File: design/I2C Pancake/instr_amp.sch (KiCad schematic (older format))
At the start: 5 parts, among them J4 Conn_01x04, U3 INA826

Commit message: Create initial 4-layer routing for I2C Pancake Board.
This is my first attempt at doing 4-layer routing. There are
some outstanding issues with the routing here. Namely, the
coupling/decoupling capacitors have rather long traces
connecting them to their respective devices. These issues
will be fixed in future commits.
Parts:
- C5: symbol i2c_pancake-rescue:C-device -> i2c_pancake-rescue:C-device-i2c_pancake-rescue
- J4: symbol i2c_pancake-rescue:Conn_01x04-strain_gauges_rtr-rescue -> i2c_pancake-rescue:Conn_01x04-strain_gauges_rtr-rescue-i2c_pancake-rescue
- R6, R7: symbol i2c_pancake-rescue:R-device -> i2c_pancake-rescue:R-device-i2c_pancake-rescue
- U3: symbol i2c_pancake-rescue:INA826-daq_components -> i2c_pancake-rescue:INA826-daq_components-i2c_pancake-rescue
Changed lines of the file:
@@
 $EndDescr
 $Comp
-L i2c_pancake-rescue:INA826-daq_components U3
+L i2c_pancake-rescue:INA826-daq_components-i2c_pancake-rescue U3
 U 1 1 5ACAFA52
 P 5900 4100
@@
 $EndComp
 $Comp
-L i2c_pancake-rescue:Conn_01x04-strain_gauges_rtr-rescue J4
+L i2c_pancake-rescue:Conn_01x04-strain_gauges_rtr-rescue-i2c_pancake-rescue J4
 U 1 1 5ACAFAD2
 P 4750 3150
@@
 	5100 3350 4950 3350
 $Comp
-L i2c_pancake-rescue:R-device R6
+L i2c_pancake-rescue:R-device-i2c_pancake-rescue R6
 U 1 1 5ACAFBC2
 P 5000 4100
@@
 	6450 3950 6350 3950
 $Comp
-L i2c_pancake-rescue:C-device C5
+L i2c_pancake-rescue:C-device-i2c_pancake-rescue C5
 U 1 1 5ACAFF7B
 P 6600 3700
@@
 AR Path="/5ACB084A/5ACAFF7B" Ref="C8"  Part="1"
 AR Path="/5E82A218/5ACAFF7B" Ref="C2"  Part="1"
+AR Path="/5ACAFF7B" Ref="C2"  Part="1"
 F 0 "C2" V 6650 3750 50  0000 L CNN
 F 1 "0.1uF" V 6550 3750 50  0000 L CNN
@@
 G = 1 + 49.4K/RG
 $Comp
-L i2c_pancake-rescue:R-device R7
+L i2c_pancake-rescue:R-device-i2c_pancake-rescue R7
 U 1 1 5ACB2059
 P 6500 4150

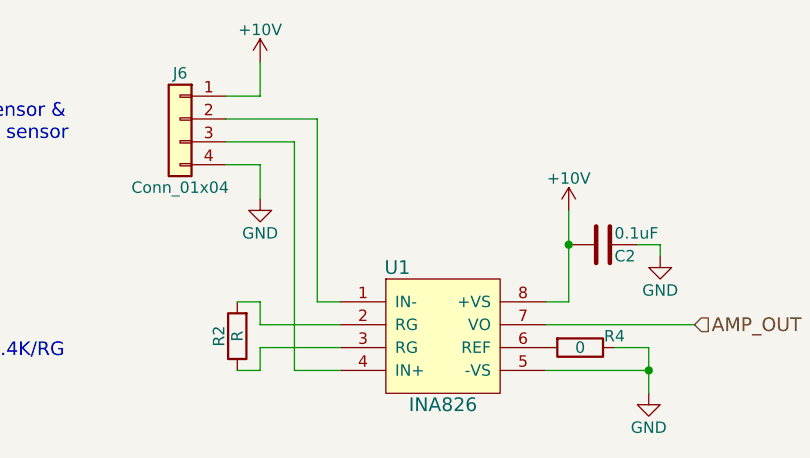
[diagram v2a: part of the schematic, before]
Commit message: Replace fuse footprint with standard 0805 SMD footprint.
A note has been added to the schematic regarding expected current
and trip current through the fuse.
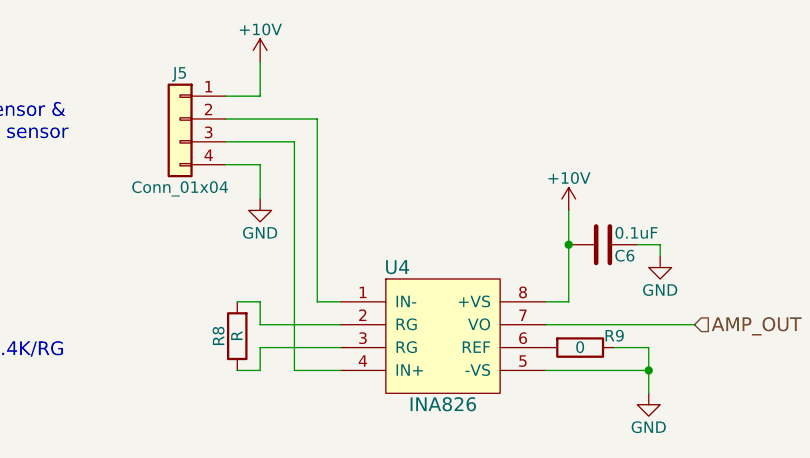
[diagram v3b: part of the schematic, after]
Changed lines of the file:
@@
 $Descr A4 11693 8268
 encoding utf-8
-Sheet 4 4
+Sheet 3 4
 Title ""
 Date ""
@@
 AR Path="/5ACB084A/5ACAFA52" Ref="U6"  Part="1"
 AR Path="/5E82A218/5ACAFA52" Ref="U1"  Part="1"
-F 0 "U1" H 5700 4400 60  0000 C CNN
+F 0 "U4" H 5700 4400 60  0000 C CNN
 F 1 "INA826" H 5900 3800 60  0000 C CNN
 F 2 "footprints:SOIC-8_3.9x4.9mm_Pitch1.27mm_HandSoldering" H 6050 3800 60  0001 C CNN
@@
 AR Path="/5ACB084A/5ACAFAD2" Ref="J7"  Part="1"
 AR Path="/5E82A218/5ACAFAD2" Ref="J6"  Part="1"
-F 0 "J6" H 4750 3350 50  0000 C CNN
+F 0 "J5" H 4750 3350 50  0000 C CNN
 F 1 "Conn_01x04" H 4750 2850 50  0000 C CNN
 F 2 "TerminalBlock_Phoenix:TerminalBlock_Phoenix_MKDS-1,5-4_1x04_P5.00mm_Horizontal" H 4750 3150 50  0001 C CNN
@@
 AR Path="/5ACB084A/5ACAFBC2" Ref="R12"  Part="1"
 AR Path="/5E82A218/5ACAFBC2" Ref="R2"  Part="1"
-F 0 "R2" V 5080 4100 50  0000 C CNN
+F 0 "R8" V 5080 4100 50  0000 C CNN
 F 1 "R" V 5000 4100 50  0000 C CNN
 F 2 "footprints:R_0805_HandSoldering" V 4930 4100 50  0001 C CNN
@@
 AR Path="/5E82A218/5ACAFF7B" Ref="C2"  Part="1"
 AR Path="/5ACAFF7B" Ref="C2"  Part="1"
-F 0 "C2" V 6650 3750 50  0000 L CNN
+F 0 "C6" V 6650 3750 50  0000 L CNN
 F 1 "0.1uF" V 6550 3750 50  0000 L CNN
 F 2 "footprints:C_0805_HandSoldering" H 6638 3550 50  0001 C CNN
@@
 AR Path="/5ACB084A/5ACB2059" Ref="R13"  Part="1"
 AR Path="/5E82A218/5ACB2059" Ref="R4"  Part="1"
-F 0 "R4" V 6450 4300 50  0000 C CNN
+F 0 "R9" V 6450 4300 50  0000 C CNN
 F 1 "0" V 6500 4150 50  0000 C CNN
 F 2 "footprints:R_0805_HandSoldering" V 6430 4150 50  0001 C CNN

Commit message: Add test points to the Pancake board.
Test points were added to the outputs of each strain guage amp.
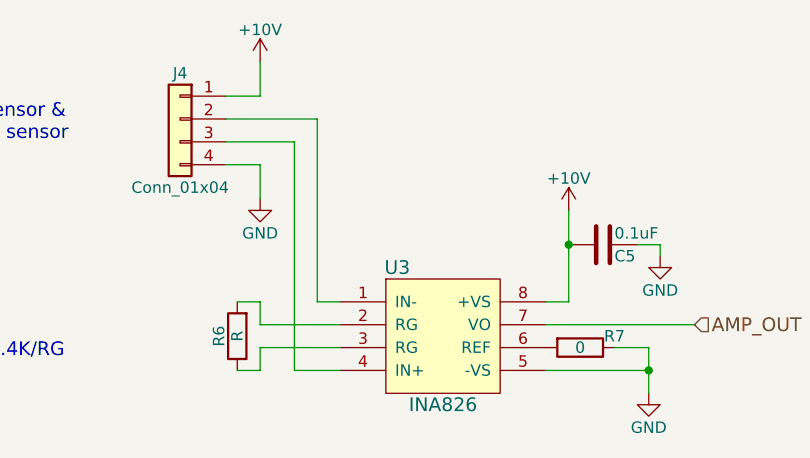
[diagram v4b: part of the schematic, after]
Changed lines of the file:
@@
 $Descr A4 11693 8268
 encoding utf-8
-Sheet 3 4
+Sheet 2 4
 Title ""
 Date ""
@@
 AR Path="/5ACB084A/5ACAFA52" Ref="U6"  Part="1"
 AR Path="/5E82A218/5ACAFA52" Ref="U1"  Part="1"
-F 0 "U4" H 5700 4400 60  0000 C CNN
+F 0 "U3" H 5700 4400 60  0000 C CNN
 F 1 "INA826" H 5900 3800 60  0000 C CNN
 F 2 "footprints:SOIC-8_3.9x4.9mm_Pitch1.27mm_HandSoldering" H 6050 3800 60  0001 C CNN
@@
 AR Path="/5ACB084A/5ACAFAD2" Ref="J7"  Part="1"
 AR Path="/5E82A218/5ACAFAD2" Ref="J6"  Part="1"
-F 0 "J5" H 4750 3350 50  0000 C CNN
+F 0 "J4" H 4750 3350 50  0000 C CNN
 F 1 "Conn_01x04" H 4750 2850 50  0000 C CNN
 F 2 "TerminalBlock_Phoenix:TerminalBlock_Phoenix_MKDS-1,5-4_1x04_P5.00mm_Horizontal" H 4750 3150 50  0001 C CNN
@@
 AR Path="/5ACB084A/5ACAFBC2" Ref="R12"  Part="1"
 AR Path="/5E82A218/5ACAFBC2" Ref="R2"  Part="1"
-F 0 "R8" V 5080 4100 50  0000 C CNN
+F 0 "R6" V 5080 4100 50  0000 C CNN
 F 1 "R" V 5000 4100 50  0000 C CNN
 F 2 "footprints:R_0805_HandSoldering" V 4930 4100 50  0001 C CNN
@@
 AR Path="/5E82A218/5ACAFF7B" Ref="C2"  Part="1"
 AR Path="/5ACAFF7B" Ref="C2"  Part="1"
-F 0 "C6" V 6650 3750 50  0000 L CNN
+F 0 "C5" V 6650 3750 50  0000 L CNN
 F 1 "0.1uF" V 6550 3750 50  0000 L CNN
 F 2 "footprints:C_0805_HandSoldering" H 6638 3550 50  0001 C CNN
@@
 AR Path="/5ACB084A/5ACB2059" Ref="R13"  Part="1"
 AR Path="/5E82A218/5ACB2059" Ref="R4"  Part="1"
-F 0 "R9" V 6450 4300 50  0000 C CNN
+F 0 "R7" V 6450 4300 50  0000 C CNN
 F 1 "0" V 6500 4150 50  0000 C CNN
 F 2 "footprints:R_0805_HandSoldering" V 6430 4150 50  0001 C CNN

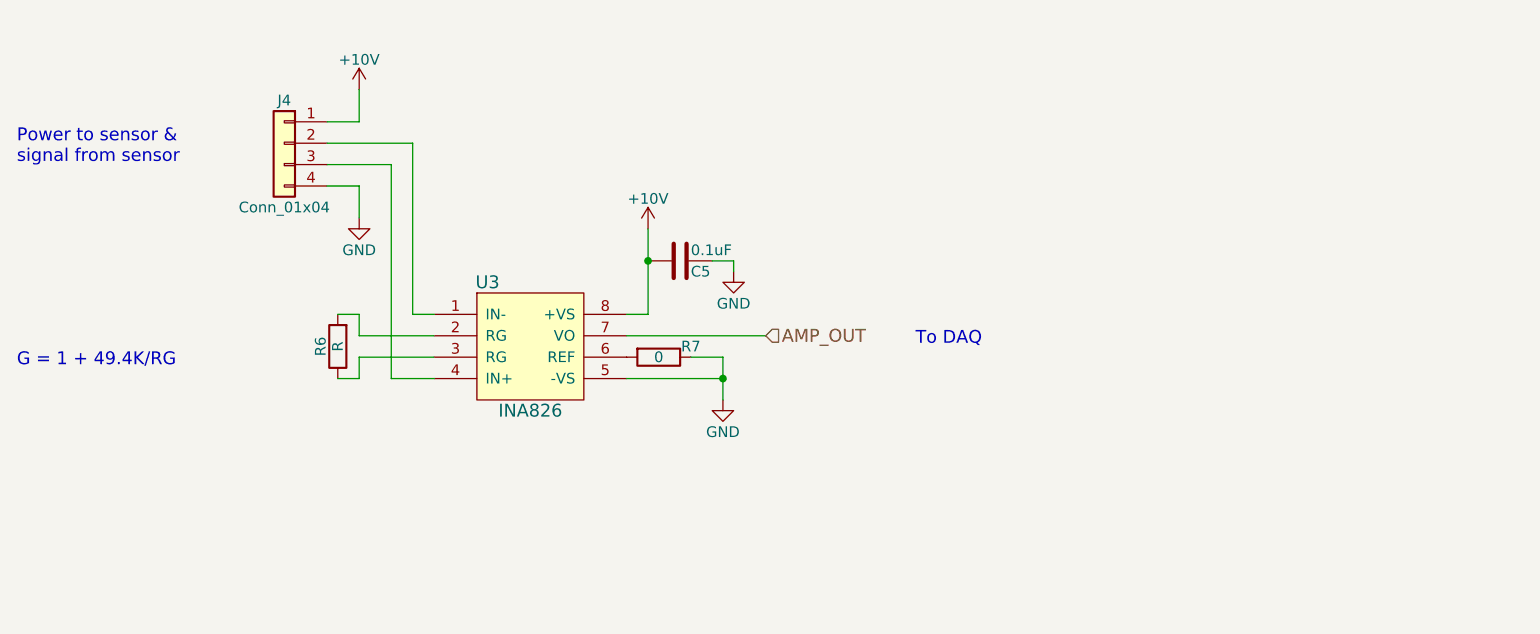
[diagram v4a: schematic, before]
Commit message: Implement improvements suggested by Zachariah Mears and update Gerbers
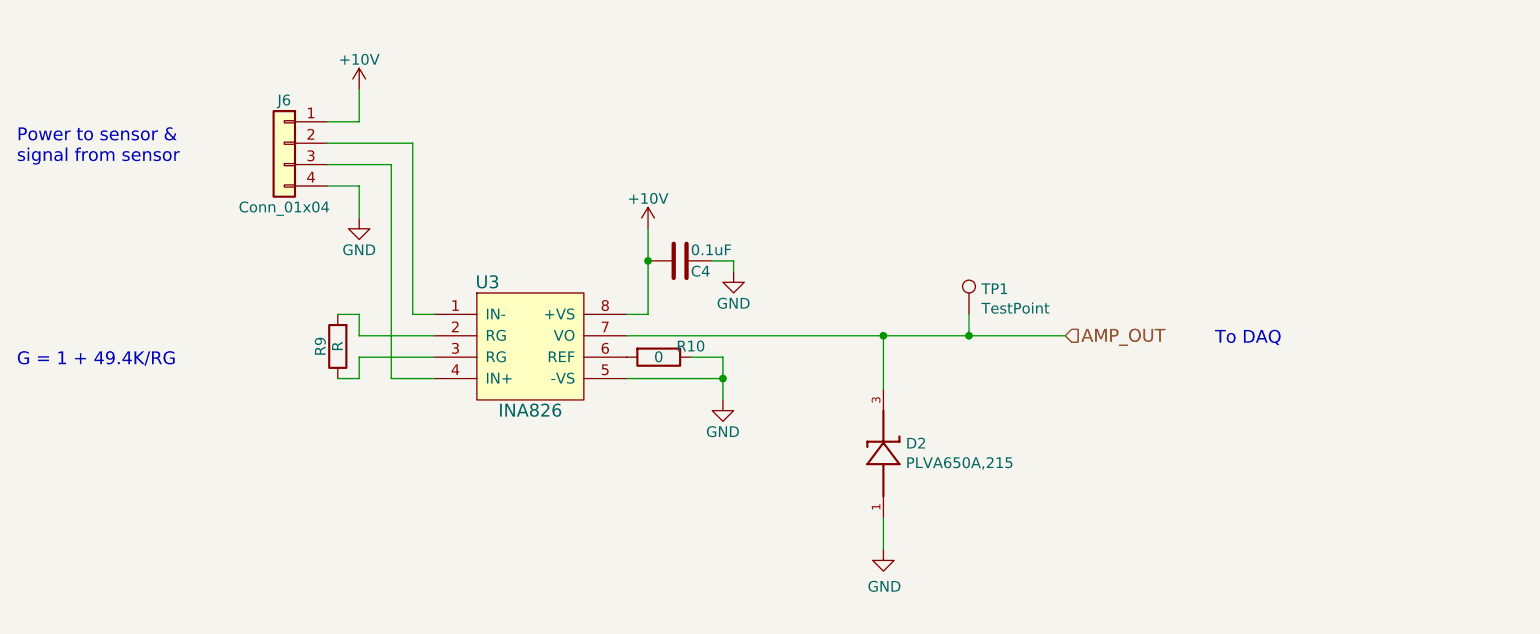
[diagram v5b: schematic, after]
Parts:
- added D2: PLVA650A,215, footprints:SOT95P230X110-3N, symbol PLVA650A_215:PLVA650A,215
- added TP1: TestPoint, custom:TestPoint, symbol Connector:TestPoint
- renumbered C5 to C4, J4 to J6, R7 to R10, R6 to R9
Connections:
- net AMP_OUT: now also D2.3, TP1.1
- net GND: now also D2.1

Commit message: Replace linear regulator to match the recent Digikey order
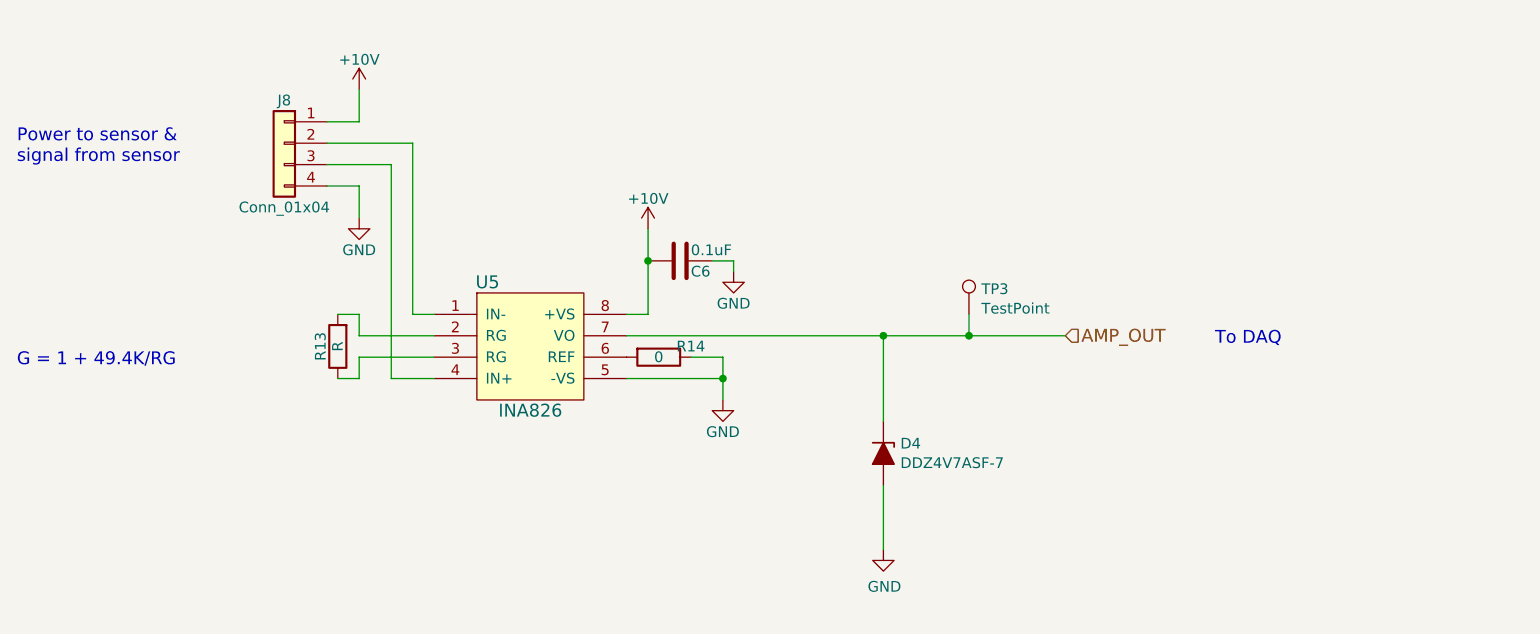
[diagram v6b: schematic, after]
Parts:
- removed D2: PLVA650A,215, footprints:SOT95P230X110-3N, symbol PLVA650A_215:PLVA650A,215
- added D2: DDZ4V7ASF-7, Diode_SMD:D_SOD-323F, symbol Device:D_Zener_ALT
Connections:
- net AMP_OUT: now also D2.1 (K)
- net GND: now also D2.2 (A)
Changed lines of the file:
@@
 $Descr A4 11693 8268
 encoding utf-8
-Sheet 2 4
+Sheet 4 4
 Title ""
 Date ""
@@
 AR Path="/5ACB084A/5ACAFA52" Ref="U?"  Part="1"
 AR Path="/5E82A218/5ACAFA52" Ref="U5"  Part="1"
-F 0 "U3" H 5700 4400 60  0000 C CNN
+F 0 "U5" H 5700 4400 60  0000 C CNN
 F 1 "INA826" H 5900 3800 60  0000 C CNN
 F 2 "footprints:SOIC-8_3.9x4.9mm_Pitch1.27mm_HandSoldering" H 6050 3800 60  0001 C CNN
@@
 AR Path="/5ACB084A/5ACAFAD2" Ref="J?"  Part="1"
 AR Path="/5E82A218/5ACAFAD2" Ref="J8"  Part="1"
-F 0 "J6" H 4750 3350 50  0000 C CNN
+F 0 "J8" H 4750 3350 50  0000 C CNN
 F 1 "Conn_01x04" H 4750 2850 50  0000 C CNN
 F 2 "TerminalBlock_Phoenix:TerminalBlock_Phoenix_MKDS-1,5-4_1x04_P5.00mm_Horizontal" H 4750 3150 50  0001 C CNN
@@
 AR Path="/5ACB084A/5ACAFB32" Ref="#PWR?"  Part="1"
 AR Path="/5E82A218/5ACAFB32" Ref="#PWR039"  Part="1"
-F 0 "#PWR027" H 5100 2750 50  0001 C CNN
+F 0 "#PWR039" H 5100 2750 50  0001 C CNN
 F 1 "+10V" H 5100 3040 50  0000 C CNN
 F 2 "" H 5100 2900 50  0000 C CNN
@@
 AR Path="/5ACB084A/5ACAFB50" Ref="#PWR?"  Part="1"
 AR Path="/5E82A218/5ACAFB50" Ref="#PWR040"  Part="1"
-F 0 "#PWR028" H 5100 3250 50  0001 C CNN
+F 0 "#PWR040" H 5100 3250 50  0001 C CNN
 F 1 "GND" H 5100 3350 50  0000 C CNN
 F 2 "" H 5100 3500 50  0001 C CNN
@@
 AR Path="/5ACB084A/5ACAFBC2" Ref="R?"  Part="1"
 AR Path="/5E82A218/5ACAFBC2" Ref="R13"  Part="1"
-F 0 "R9" V 5080 4100 50  0000 C CNN
+F 0 "R13" V 5080 4100 50  0000 C CNN
 F 1 "R" V 5000 4100 50  0000 C CNN
 F 2 "footprints:R_0805_HandSoldering" V 4930 4100 50  0001 C CNN
@@
 AR Path="/5ACB084A/5ACAFF30" Ref="#PWR?"  Part="1"
 AR Path="/5E82A218/5ACAFF30" Ref="#PWR041"  Part="1"
-F 0 "#PWR029" H 6450 3400 50  0001 C CNN
+F 0 "#PWR041" H 6450 3400 50  0001 C CNN
 F 1 "+10V" H 6450 3690 50  0000 C CNN
 F 2 "" H 6450 3550 50  0000 C CNN
@@
 AR Path="/5E82A218/5ACAFF7B" Ref="C6"  Part="1"
 AR Path="/5ACAFF7B" Ref="C?"  Part="1"
-F 0 "C4" V 6650 3750 50  0000 L CNN
+F 0 "C6" V 6650 3750 50  0000 L CNN
 F 1 "0.1uF" V 6550 3750 50  0000 L CNN
 F 2 "footprints:C_0805_HandSoldering" H 6638 3550 50  0001 C CNN
@@
 AR Path="/5ACB084A/5ACB002E" Ref="#PWR?"  Part="1"
 AR Path="/5E82A218/5ACB002E" Ref="#PWR043"  Part="1"
-F 0 "#PWR031" H 6850 3500 50  0001 C CNN
+F 0 "#PWR043" H 6850 3500 50  0001 C CNN
 F 1 "GND" H 6850 3600 50  0000 C CNN
 F 2 "" H 6850 3750 50  0001 C CNN
@@
 AR Path="/5ACB084A/5ACB0087" Ref="#PWR?"  Part="1"
 AR Path="/5E82A218/5ACB0087" Ref="#PWR042"  Part="1"
-F 0 "#PWR030" H 6800 4100 50  0001 C CNN
+F 0 "#PWR042" H 6800 4100 50  0001 C CNN
 F 1 "GND" H 6800 4200 50  0000 C CNN
 F 2 "" H 6800 4350 50  0001 C CNN
@@
 AR Path="/5ACB084A/5ACB2059" Ref="R?"  Part="1"
 AR Path="/5E82A218/5ACB2059" Ref="R14"  Part="1"
-F 0 "R10" V 6450 4300 50  0000 C CNN
+F 0 "R14" V 6450 4300 50  0000 C CNN
 F 1 "0" V 6500 4150 50  0000 C CNN
 F 2 "footprints:R_0805_HandSoldering" V 6430 4150 50  0001 C CNN
@@
 Wire Wire Line
 	6800 4250 6800 4150
-$Comp
-L PLVA650A_215:PLVA650A,215 D2
-U 1 1 5F7133A6
-P 7550 4600
-AR Path="/5ACAF8FB/5F7133A6" Ref="D2"  Part="1"
-AR Path="/5ACB06D8/5F7133A6" Ref="D3"  Part="1"
-AR Path="/5E82A218/5F7133A6" Ref="D4"  Part="1"
-F 0 "D2" V 7596 4495 50  0000 R CNN
-F 1 "PLVA650A,215" V 7505 4495 50  0000 R CNN
-F 2 "footprints:SOT95P230X110-3N" H 7550 4600 50  0001 L BNN
-F 3 "Good" H 7550 4600 50  0001 L BNN
-F 4 "PLVA650A,215" H 7550 4600 50  0001 L BNN "Field4"
-F 5 "$0.13 USD" H 7550 4600 50  0001 L BNN "Field5"
-F 6 "SOT95P230X110-3N" H 7550 4600 50  0001 L BNN "Field6"
-F 7 "NXP" H 7550 4600 50  0001 L BNN "Field7"
-	1    7550 4600
-	0    -1   -1   0
-$EndComp
 $Comp
 L power:GND #PWR032
@@
 AR Path="/5ACB06D8/5F714D6C" Ref="#PWR038"  Part="1"
 AR Path="/5E82A218/5F714D6C" Ref="#PWR044"  Part="1"
-F 0 "#PWR032" H 7550 4800 50  0001 C CNN
+F 0 "#PWR044" H 7550 4800 50  0001 C CNN
 F 1 "GND" H 7555 4877 50  0000 C CNN
 F 2 "" H 7550 5050 50  0001 C CNN
@@
 	1    0    0    -1
 $EndComp
-Wire Wire Line
-	7550 4300 7550 4050
 Connection ~ 7550 4050
 Wire Wire Line
 	7550 4050 7950 4050
-Wire Wire Line
-	7550 5050 7550 4900
 Wire Wire Line
 	6350 4050 7550 4050
@@
 AR Path="/5ACB06D8/5F718F0E" Ref="TP2"  Part="1"
 AR Path="/5E82A218/5F718F0E" Ref="TP3"  Part="1"
-F 0 "TP1" H 8008 4068 50  0000 L CNN
+F 0 "TP3" H 8008 4068 50  0000 L CNN
 F 1 "TestPoint" H 8008 3977 50  0000 L CNN
 F 2 "custom:TestPoint" H 8150 3950 50  0001 C CNN
@@
 Wire Wire Line
 	7950 3950 7950 4050
+$Comp
+L Device:D_Zener_ALT D2
+U 1 1 5F752324
+P 7550 4600
+AR Path="/5ACAF8FB/5F752324" Ref="D2"  Part="1"
+AR Path="/5ACB06D8/5F752324" Ref="D3"  Part="1"
+AR Path="/5E82A218/5F752324" Ref="D4"  Part="1"
+F 0 "D4" V 7504 4679 50  0000 L CNN
+F 1 "DDZ4V7ASF-7" V 7595 4679 50  0000 L CNN
+F 2 "Diode_SMD:D_SOD-323F" H 7550 4600 50  0001 C CNN
+F 3 "~" H 7550 4600 50  0001 C CNN
+	1    7550 4600
+	0    1    1    0
+$EndComp
+Wire Wire Line
+	7550 4050 7550 4450
+Wire Wire Line
+	7550 4750 7550 5050
 $EndSCHEMATC

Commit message: Add RC filters to the analog inputs of the PIC
This commit also includes a new and improved routing.
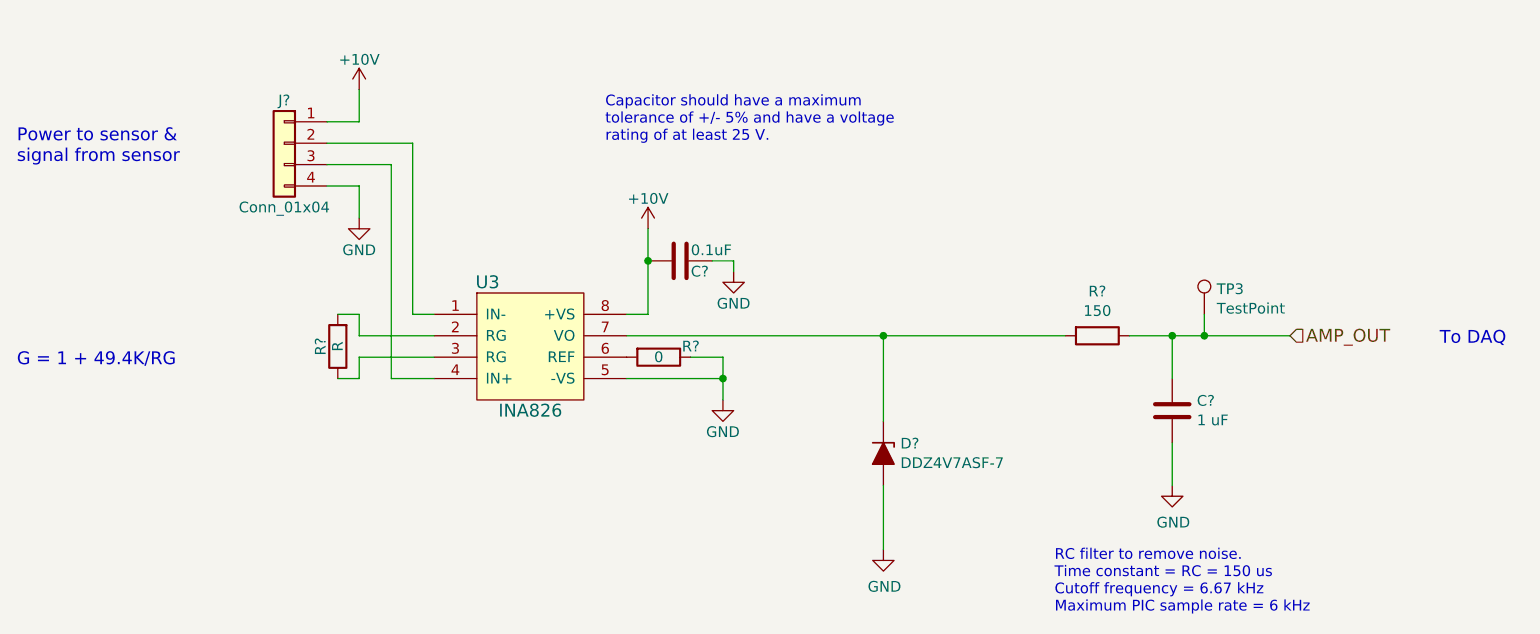
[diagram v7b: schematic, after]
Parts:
- added C?: 1 uF, footprints:C_0805_HandSoldering, symbol Device:C
- added R?: 150, footprints:R_0805_HandSoldering, symbol Device:R
- renumbered C4 to C?, D2 to D?, J6 to J?, R9 to R?, R10 to R?, U3 to U1
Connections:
- net AMP_OUT: now also C?.1, R?.1; no longer D?.1 (K), U1.7 (VO)
- net GND: now also C?.2
- new net: D?.1 (K), R?.2, U1.7 (VO)
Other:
- note added: "Capacitor should have a maximum\ntolerance of +/- 5% and have a voltage\nrating of at least 25 V."
- note added: "RC filter to remove noise. \nTime constant = RC = 150 us\nCutoff frequency = 6.67 kHz\nMaximum PIC sample rate = 6 kHz"
- moved on the sheet: TP3
